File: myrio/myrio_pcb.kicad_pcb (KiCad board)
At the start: 4 copper layers, 191.1 x 89.5 mm, 136 parts, among them J1 DB9, P1 CONN_02X17, P2 CONN_02X17, Q1 PN2222A, Q10 PN2222A, Q11 PN2222A, Q12 PN2222A, Q13 PN2222A, Q14 PN2222A, Q15 PN2222A, Q16 PN2222A, Q17 PN2222A, Q18 PN2222A, Q19 PN2222A, Q2 PN2222A, Q20 PN2222A, Q21 PN2222A, Q3 PN2222A, Q4 PN2222A, Q5 PN2222A, Q6 PN2222A, Q7 PN2222A, Q8 PN2222A, Q9 PN2222A, U1 stacked-DB9, U10 INA219, U11 INA219, U13 INA219, U14 stacked-rj45-LED, U15 stacked-rj45-LED, U16 12V regulator, U2 stacked-DB9, U3 stacked-rj45-LED, U4 stacked-rj45-LED, U5 stacked-rj45-LED, U6 BNO055, U7 stacked-rj45-LED, U9 LM1084IT-5.0/NOPB

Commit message: moved the readme over here
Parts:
- removed C1, C2, C3, C4: CP1, Capacitors_THT:CP_Radial_Tantal_D4.5mm_P2.50mm
- removed D23: D, Diodes_THT:D_DO-35_SOD27_P5.08mm_Vertical_AnodeUp
- removed Q21: PN2222A, footprints:pn2222
- removed R21: 100K, Resistors_THT:R_Axial_DIN0204_L3.6mm_D1.6mm_P5.08mm_Horizontal
- removed R31: R, Resistors_THT:R_Axial_DIN0204_L3.6mm_D1.6mm_P5.08mm_Horizontal
- removed RE21: relay, footprints:relay
- removed the REF** at (198.1, 47.0)
- removed the REF** at (30.5, 48.9)
- removed the REF** at (198.8, 101.6)
- removed the REF** at (37.5, 101.6)
- removed U16: 12V regulator, TO_SOT_Packages_THT:TO-220_Vertical
- removed U9: LM1084IT-5.0/NOPB, TO_SOT_Packages_THT:TO-220_Vertical
- added J2: CONN_02X03, Pin_Headers:Pin_Header_Straight_2x03_Pitch2.54mm, F.Cu at (209.6, 74.9)
- added J3: CONN_02X03, Pin_Headers:Pin_Header_Straight_2x03_Pitch2.54mm, F.Cu at (209.6, 64.8)
- added J4: CONN_02X03, Pin_Headers:Pin_Header_Straight_2x03_Pitch2.54mm, F.Cu at (209.6, 54.6)
- added REF**: 1pin, Connectors:1pin, F.Cu at (24.1, 48.3)
- added REF**: 1pin, Connectors:1pin, F.Cu at (201.9, 45.7)
- added REF**: 1pin, Connectors:1pin, F.Cu at (38.7, 101.6)
- added REF**: 1pin, Connectors:1pin, F.Cu at (226.1, 101.0)
- added S11: 2pinscrew, footprints:screwinconnector++, F.Cu at (226.7, 59.1)
- added U8: stacked-DB9, footprints:DB9-doublestacked_PR, F.Cu at (208.5, 33.5)
- H1: footprint footprints:bmp180_ref -> footprints:bmp180
- J1: value DB9 -> CONN_02X03; footprint Connectors:DB9FD -> Pin_Headers:Pin_Header_Straight_2x03_Pitch2.54mm
- Q1, Q10, Q11, Q12, Q13, Q14, Q15, Q16, Q17, Q18, Q19, Q2, Q20, Q3, Q4, Q5, Q6, Q7, Q8, Q9: footprint footprints:pn2222 -> TO_SOT_Packages_THT:TO-92_Inline_Narrow_Oval
- S1, S10, S2, S3, S4, S5, S6, S7, S8, S9: footprint footprints:screwinconnector -> footprints:screwinconnector++
- U14, U15, U3, U4, U5, U7: footprint footprints:stacked-rj45_Final -> footprints:stacked-rj45_Final++
- moved S10 204.9 mm to (226.7, 93.3)
- moved S9 204.8 mm to (226.7, 81.9)
- moved S8 204.7 mm to (226.7, 70.5)
- moved S2 184.4 mm to (23.7, 85.6)
- moved S5 183.8 mm to (23.7, 74.2), turned to 270 degrees
- moved S4 183.5 mm to (23.7, 62.7)
- moved J1 58.6 mm to (209.6, 85.1), turned to 0 degrees
- moved S1 48.9 mm to (214.0, 102.2), turned to 0 degrees
- moved D21 20.0 mm to (169.2, 99.8), turned to 180 degrees
- moved S7 14.0 mm to (191.1, 102.2)
- moved S3 12.7 mm to (179.7, 102.2)
- moved D22 11.3 mm to (201.9, 87.6), turned to 270 degrees
- moved U1 7.63 mm to (154.3, 39.0)
- moved U2 7.63 mm to (188.0, 39.0)
- moved U15 6.99 mm to (132.1, 30.5)
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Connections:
- 220ohm1 pad 2: friction_gnd -> DGND
- 220ohm2 pad 2: friction_gnd -> DGND
- 220ohm3 pad 2: friction_gnd -> DGND
- 220ohm4 pad 2: friction_gnd -> DGND
- J1 pad 1: Net-(J1-Pad1) -> non_critical_scl
- J1 pad 2: Net-(J1-Pad2) -> i2c_scl_2
- J1 pad 3: Net-(J1-Pad3) -> tof_scl
- J1 pad 4: Net-(J1-Pad4) -> tof_scl
- J1 pad 5: friction_gnd -> (no net)
- J1 pad 6: Net-(J1-Pad6) -> critical_scl
- P1 pad 1: Net-(P1-Pad1) -> (no net)
- P1 pad 10: Net-(P1-Pad10) -> (no net)
- P1 pad 12: friction_gnd -> DGND
- P1 pad 14: Net-(P1-Pad14) -> (no net)
- P1 pad 16: friction_gnd -> DGND
- P1 pad 2: Net-(P1-Pad2) -> (no net)
- P1 pad 20: friction_gnd -> DGND
- P1 pad 24: friction_gnd -> DGND
- P1 pad 28: friction_gnd -> DGND
- P1 pad 30: friction_gnd -> DGND
- P1 pad 33: Net-(P1-Pad33) -> (no net)
- P1 pad 4: Net-(P1-Pad4) -> (no net)
- P1 pad 6: friction_gnd -> DGND
- P1 pad 8: friction_gnd -> DGND
- P2 pad 1: Net-(P2-Pad1) -> (no net)
- P2 pad 10: Net-(P2-Pad10) -> (no net)
- P2 pad 14: Net-(P2-Pad14) -> (no net)
- P2 pad 2: Net-(P2-Pad2) -> (no net)
- P2 pad 33: Net-(P2-Pad33) -> (no net)
- P2 pad 4: Net-(P2-Pad4) -> (no net)
- P2 pad 6: friction_gnd -> DGND
- P2 pad 7: Net-(P2-Pad7) -> (no net)
- P2 pad 9: Net-(P2-Pad9) -> (no net)
- Q1 pad 1: friction_gnd -> DGND
- Q10 pad 1: friction_gnd -> DGND
- Q11 pad 1: friction_gnd -> DGND
- Q12 pad 1: friction_gnd -> DGND
- Q13 pad 1: friction_gnd -> DGND
- Q14 pad 1: friction_gnd -> DGND
- Q15 pad 1: friction_gnd -> DGND
- Q16 pad 1: friction_gnd -> DGND
- Q17 pad 1: friction_gnd -> DGND
- Q18 pad 1: friction_gnd -> DGND
- Q19 pad 1: friction_gnd -> DGND
- Q2 pad 1: friction_gnd -> DGND
- Q20 pad 1: friction_gnd -> DGND
- Q3 pad 1: friction_gnd -> DGND
- Q4 pad 1: friction_gnd -> DGND
- Q5 pad 1: friction_gnd -> DGND
- Q6 pad 1: friction_gnd -> DGND
- Q7 pad 1: friction_gnd -> DGND
- Q8 pad 1: friction_gnd -> DGND
- Q9 pad 1: friction_gnd -> DGND
- RE1 pad 5: Net-(RE1-Pad5) -> (no net)
- RE10 pad 5: Net-(RE10-Pad5) -> (no net)
- RE11 pad 5: Net-(RE11-Pad5) -> (no net)
- RE12 pad 5: Net-(RE12-Pad5) -> (no net)
- RE13 pad 6: Net-(RE13-Pad6) -> (no net)
- RE15 pad 6: Net-(RE15-Pad6) -> (no net)
- RE18 pad 10: Net-(RE18-Pad10) -> (no net)
- RE19 pad 1: friction_gnd -> DGND
- RE2 pad 5: Net-(RE2-Pad5) -> (no net)
- RE20 pad 1: friction_gnd -> DGND
- RE3 pad 5: Net-(RE3-Pad5) -> (no net)
- RE4 pad 5: Net-(RE4-Pad5) -> (no net)
- RE5 pad 1: Net-(RE5-Pad1) -> (no net)
- RE9 pad 5: Net-(RE9-Pad5) -> (no net)
- S1 pad 1: VCC_IN -> batt_in
- S1 pad 2: friction_gnd -> DGND
- S10 pad 1: 5V -> 12V
- S10 pad 2: friction_gnd -> DGND
- S6 pad 2: friction_gnd -> DGND
- S7 pad 1: motor_pwr -> 24V
- S7 pad 2: friction_gnd -> magnetic_pwr
- S8 pad 1: VCC_IN -> 12V
- S8 pad 2: friction_gnd -> DGND
- S9 pad 1: 12V -> DGND
- S9 pad 2: friction_gnd -> 24V
- U1 pad 14: friction_gnd -> DGND
- U1 pad 15: friction_gnd -> DGND
- U1 pad 16: friction_gnd -> DGND
- U1 pad 17: friction_gnd -> DGND
- U1 pad 18: friction_gnd -> DGND
- U1 pad 5: friction_gnd -> DGND
- U1 pad 6: friction_gnd -> DGND
- U1 pad 7: friction_gnd -> DGND
- U1 pad 8: friction_gnd -> DGND
- U1 pad 9: friction_gnd -> DGND
- U10 pad 5: Net-(U10-Pad5) -> (no net)
- U10 pad 6: Net-(U10-Pad6) -> (no net)
- U11 pad 5: Net-(U11-Pad5) -> (no net)
- U11 pad 6: Net-(U11-Pad6) -> (no net)
- U11 pad 7: 24V -> 12V
- U11 pad 8: VCC_IN -> batt_in
- U13 pad 5: Net-(U13-Pad5) -> (no net)
- U13 pad 6: Net-(U13-Pad6) -> (no net)
- U14 pad 14: Net-(U14-Pad14) -> (no net)
- U14 pad 17: Net-(U14-Pad17) -> (no net)
- U14 pad 18: Net-(U14-Pad18) -> (no net)
- U14 pad 19: Net-(U14-Pad19) -> (no net)
- U14 pad 20: Net-(U14-Pad20) -> (no net)
- U14 pad 21: Net-(U14-Pad21) -> (no net)
- U14 pad 22: Net-(U14-Pad22) -> (no net)
- U14 pad 23: Net-(U14-Pad23) -> (no net)
- U14 pad 24: Net-(U14-Pad24) -> (no net)
- U14 pad 6: Net-(U14-Pad6) -> (no net)
- U14 pad 8: Net-(U14-Pad8) -> (no net)
- U15 pad 12: Net-(U15-Pad12) -> (no net)
- U15 pad 13: Net-(U15-Pad13) -> (no net)
- U15 pad 15: Net-(U15-Pad15) -> (no net)
- U15 pad 16: Net-(U15-Pad16) -> (no net)
- U15 pad 17: Net-(U15-Pad17) -> (no net)
- U15 pad 18: Net-(U15-Pad18) -> (no net)
- U15 pad 19: Net-(U15-Pad19) -> (no net)
- U15 pad 20: Net-(U15-Pad20) -> (no net)
- U15 pad 21: Net-(U15-Pad21) -> (no net)
- U15 pad 22: Net-(U15-Pad22) -> (no net)
- U15 pad 23: Net-(U15-Pad23) -> (no net)
- U15 pad 24: Net-(U15-Pad24) -> (no net)
- U2 pad 14: friction_gnd -> DGND
- U2 pad 15: friction_gnd -> DGND
- U2 pad 16: friction_gnd -> DGND
- U2 pad 17: friction_gnd -> DGND
- U2 pad 18: friction_gnd -> DGND
- U2 pad 5: friction_gnd -> DGND
- U2 pad 6: friction_gnd -> DGND
- U2 pad 7: friction_gnd -> DGND
- U2 pad 8: friction_gnd -> DGND
- U2 pad 9: friction_gnd -> DGND
- U3 pad 17: Net-(U3-Pad17) -> (no net)
- U3 pad 18: Net-(U3-Pad18) -> (no net)
- U3 pad 19: Net-(U3-Pad19) -> (no net)
- U3 pad 20: Net-(U3-Pad20) -> (no net)
- U3 pad 21: Net-(U3-Pad21) -> (no net)
- U3 pad 22: Net-(U3-Pad22) -> (no net)
- U3 pad 23: Net-(U3-Pad23) -> (no net)
- U3 pad 24: Net-(U3-Pad24) -> (no net)
- U4 pad 11: non_critical_scl -> tof_scl
- U4 pad 14: non_critical_sda -> tof_sda
- U4 pad 15: non_critical_scl -> tof_scl
- U4 pad 16: non_critical_sda -> tof_sda
- U4 pad 17: Net-(U4-Pad17) -> (no net)
- U4 pad 18: Net-(U4-Pad18) -> (no net)
- U4 pad 19: Net-(U4-Pad19) -> (no net)
- U4 pad 20: Net-(U4-Pad20) -> (no net)
- U4 pad 21: Net-(U4-Pad21) -> (no net)
- U4 pad 22: Net-(U4-Pad22) -> (no net)
- U4 pad 23: Net-(U4-Pad23) -> (no net)
- U4 pad 24: Net-(U4-Pad24) -> (no net)
- U4 pad 3: critical_scl -> tof_scl
- U4 pad 6: critical_sda -> tof_sda
- U4 pad 7: non_critical_scl -> tof_scl
- U4 pad 8: non_critical_sda -> tof_sda
- U5 pad 11: non_critical_scl -> stress_scl
- U5 pad 14: non_critical_sda -> stress_sda
- U5 pad 15: non_critical_scl -> stress_scl
- U5 pad 16: non_critical_sda -> stress_sda
- U5 pad 17: Net-(U5-Pad17) -> (no net)
- U5 pad 18: Net-(U5-Pad18) -> (no net)
- U5 pad 19: Net-(U5-Pad19) -> (no net)
- U5 pad 20: Net-(U5-Pad20) -> (no net)
- U5 pad 21: Net-(U5-Pad21) -> (no net)
- U5 pad 22: Net-(U5-Pad22) -> (no net)
- U5 pad 23: Net-(U5-Pad23) -> (no net)
- U5 pad 24: Net-(U5-Pad24) -> (no net)
- U5 pad 3: critical_scl -> stress_scl
- U5 pad 6: critical_sda -> stress_sda
- U5 pad 7: non_critical_scl -> stress_scl
- U5 pad 8: non_critical_sda -> stress_sda
- U6 pad 10: Net-(U6-Pad10) -> (no net)
- U6 pad 2: Net-(U6-Pad2) -> (no net)
- U6 pad 6: Net-(U6-Pad6) -> (no net)
- U6 pad 7: Net-(U6-Pad7) -> (no net)
- U6 pad 8: Net-(U6-Pad8) -> (no net)
- U6 pad 9: Net-(U6-Pad9) -> (no net)
- U7 pad 14: Net-(U7-Pad14) -> (no net)
- U7 pad 16: Net-(U7-Pad16) -> (no net)
- U7 pad 17: Net-(U7-Pad17) -> (no net)
- U7 pad 18: Net-(U7-Pad18) -> (no net)
- U7 pad 19: Net-(U7-Pad19) -> (no net)
- U7 pad 20: Net-(U7-Pad20) -> (no net)
- U7 pad 21: Net-(U7-Pad21) -> (no net)
- U7 pad 22: Net-(U7-Pad22) -> (no net)
- U7 pad 23: Net-(U7-Pad23) -> (no net)
- U7 pad 24: Net-(U7-Pad24) -> (no net)
- U7 pad 4: Net-(U7-Pad4) -> (no net)
- U7 pad 5: Net-(U7-Pad5) -> (no net)
- U7 pad 6: Net-(U7-Pad6) -> (no net)
- U7 pad 7: Net-(U7-Pad7) -> (no net)
- U7 pad 8: Net-(U7-Pad8) -> (no net)
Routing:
- net VCC_IN: track 252.3 -> 0.00 mm, vias 8 -> 0
- net tof_scl: track 0.00 -> 232.0 mm, vias 0 -> 3
- net tof_sda: track 0.00 -> 216.9 mm, vias 0 -> 6
- net stress_scl: track 0.00 -> 212.6 mm, vias 0 -> 3
- net stress_sda: track 0.00 -> 209.0 mm, vias 0 -> 2
- net friction_gnd: track 195.1 -> 0.00 mm, vias 5 -> 0
- net A0: track 203.5 -> 45.1 mm, vias 1 -> 2
- net critical_sda: track 151.8 -> 307.0 mm, vias 4 -> 6
- net A1: track 197.0 -> 43.5 mm, vias 1 -> 3
- net critical_scl: track 152.4 -> 296.7 mm, vias 1 -> 4
- net i2c_sda_2: track 167.9 -> 279.5 mm, vias 5 -> 7
- net i2c_scl_2: track 179.6 -> 289.1 mm, vias 5 -> 8
- net motor_ctrl: track 55.7 -> 152.5 mm, vias 5 -> 3
- net motor_pwr: track 96.0 -> 0.00 mm, vias 2 -> 0
- net 24V: track 86.6 -> 6.35 mm, vias 3 -> 1
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- added copper zone on B.Cu, net 24V
- removed copper zone on F.Cu, net 24V
- removed copper zone on B.Cu, net friction_gnd
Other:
- board size 191.1 x 89.5 mm -> 212 x 89.5 mm
- board text added: "Battery Sensor"
- board text added: "Brake Sensor"
- board text added: "Josh Cristol Cody Horton"
- board text added: "Mpwr"
- board text added: "MyRio Sensor"
- board text added: "NonC"
- board text added: "SCL2"
- board text added: "SCL3"
- board text added: "SDA2"
- board text added: "SDA3"
- board text added: "WE BUILD SHIT"
- board text added: "Zener Diode"
- board text added: "crit"
- board text added: "myRio+"
- board text added: "scl"
- board text added: "sda"
- board text added: "stress"
- board text added: "tof"
- board text added: "vcc"
- board text removed: "Dgnd"
- board text removed: "Motor"
- board text removed: "Regulator"
- board text removed: "WE BUILD SHIT."
- board text removed: "a0 a1 4 digital i2c lines"
- board text removed: "cap gnd move next to motor gnd screw terminals"
- board text removed: "myRio"
- board text removed: "power- battery connection and converters battery+ bat- 4 connectors for 24V booster 4 connectors for 5V booster"
- board text removed: "scl3"
- board text removed: "sda3"

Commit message: layout done, still tracing
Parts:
- removed D21: ZENER, Discret:D3
- removed the REF** at (24.1, 48.3)
- removed the REF** at (201.9, 45.7)
- removed the REF** at (38.7, 101.6)
- removed the REF** at (226.1, 101.0)
- removed S10, S11, S3, S7, S8, S9: 2pinscrew, footprints:screwinconnector++
- added D23: LED, LEDs:LED_D5.0mm, F.Cu at (212.1, 90.7)
- added R21: 500, Resistors_THT:R_Axial_DIN0204_L3.6mm_D1.6mm_P5.08mm_Horizontal, F.Cu at (208.1, 88.2)
- added R31: 12K, Resistors_THT:R_Axial_DIN0204_L3.6mm_D1.6mm_P5.08mm_Horizontal, F.Cu at (32.0, 95.2)
- added R32: 2K, Resistors_THT:R_Axial_DIN0204_L3.6mm_D1.6mm_P5.08mm_Horizontal, F.Cu at (37.0, 98.2)
- added R33: 2K, Resistors_THT:R_Axial_DIN0204_L3.6mm_D1.6mm_P5.08mm_Horizontal, F.Cu at (37.1, 104.8)
- added REF**: 1pin, Connectors:1pin, F.Cu at (23.1, 106.2)
- added REF**: 1pin, Connectors:1pin, F.Cu at (235.1, 106.2)
- added REF**: 1pin, Connectors:1pin, F.Cu at (23.1, 48.2)
- added REF**: 1pin, Connectors:1pin, F.Cu at (223.1, 46.2)
- added T1: Phoenix_Contact_1935187, footprints:Phoenix_Contact_1935187, F.Cu at (230.1, 83.7)
- added T2: Phoenix_Contact_1935187, footprints:Phoenix_Contact_1935187, F.Cu at (191.8, 100.2)
- added T3: Phoenix_Contact_1935187, footprints:Phoenix_Contact_1935187, F.Cu at (230.1, 63.2)
- added T4: Phoenix_Contact_1935187, footprints:Phoenix_Contact_1935187, F.Cu at (212.1, 100.2)
- P1, P2: moved to B.Cu
- R30: value R -> 12K
- S1: value 2pinscrew -> L101011MS02Q; footprint footprints:screwinconnector++ -> footprints:L101011MS02Q
- moved P1 65.9 mm to (169.4, 102.0)
- moved P2 65.9 mm to (112.2, 102.0)
- moved R29 59.7 mm to (42.0, 100.2), turned to 270 degrees
- moved R28 59.2 mm to (45.0, 100.2), turned to 270 degrees
- moved R22 26.1 mm to (63.0, 100.2), turned to 270 degrees
- moved S1 24.9 mm to (238.1, 95.7), turned to 90 degrees
- moved R23 21.5 mm to (60.0, 100.2), turned to 270 degrees
- moved R30 19.6 mm to (32.0, 102.2)
- moved S6 19.2 mm to (183.6, 105.2)
- moved U8 14.2 mm to (221.6, 39.0), turned to 180 degrees
- moved R24 11.0 mm to (51.0, 100.2), turned to 270 degrees
- moved R26 9.71 mm to (57.0, 100.2), turned to 270 degrees
- moved J1 7.02 mm to (210.1, 78.1)
- moved J2 7.02 mm to (210.1, 67.9)
- moved J4 7.02 mm to (210.1, 47.6)
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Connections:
- net batt_in renamed battery_sensor_input
- net laser_digital renamed laser_digital1
- net main_laser renamed main_laser1
- P2 pad 7: (no net) -> laser_digital2
- RE1 pad 1: 5V -> DGND
- RE1 pad 10: DGND -> 5V
- RE10 pad 1: 5V -> DGND
- RE10 pad 10: DGND -> 5V
- RE11 pad 1: 5V -> DGND
- RE11 pad 10: DGND -> 5V
- RE12 pad 1: 5V -> DGND
- RE12 pad 10: DGND -> 5V
- RE17 pad 1: 5V -> DGND
- RE17 pad 10: DGND -> 5V
- RE18 pad 1: to_cap -> (no net)
- RE18 pad 10: (no net) -> to_cap
- RE2 pad 1: 5V -> DGND
- RE2 pad 10: DGND -> 5V
- RE3 pad 1: 5V -> DGND
- RE3 pad 10: DGND -> 5V
- RE4 pad 1: 5V -> DGND
- RE4 pad 10: DGND -> 5V
- RE6 pad 1: 2way_open_1 -> 2way_close_1
- RE6 pad 10: 2way_close_1 -> 2way_open_1
- RE7 pad 1: 2way_open_2 -> 2way_close_2
- RE7 pad 10: 2way_close_2 -> 2way_open_2
- RE8 pad 1: 2way_open_3 -> 2way_close_3
- RE8 pad 10: 2way_close_3 -> 2way_open_3
- RE9 pad 1: 5V -> DGND
- RE9 pad 10: DGND -> 5V
- S1 pad 2: DGND -> battery+fuse
- U7 pad 4: (no net) -> 24V
- U7 pad 5: (no net) -> DGND
- U7 pad 7: (no net) -> main_laser2
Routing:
- net critical_sda: track 307.0 -> 19.3 mm, vias 6 -> 0
- net i2c_scl_2: track 289.1 -> 34.9 mm, vias 8 -> 0
- net i2c_sda_2: track 279.5 -> 26.4 mm, vias 7 -> 0
- net critical_scl: track 296.7 -> 96.2 mm, vias 4 -> 2
- net tof_sda: track 216.9 -> 21.2 mm, vias 6 -> 1
- net stress_scl: track 212.6 -> 22.5 mm, vias 3 -> 0
- net tof_scl: track 232.0 -> 78.2 mm, vias 3 -> 1
- net motor_ctrl: track 152.5 -> 0.00 mm, vias 3 -> 0
- net non_critical_sda: track 307.3 -> 178.0 mm, vias 8 -> 5
- net laser_digital1: track 123.4 -> 2.61 mm, vias 3 -> 0
- net laser2: track 96.6 -> 0.00 mm, vias 4 -> 0
- net sense_pwr_ctrl: track 89.4 -> 0.00 mm, vias 5 -> 0
- net pressure_activation: track 85.5 -> 0.06 mm, vias 3 -> 0
- net magnetic_ctrl: track 83.6 -> 0.00 mm, vias 1 -> 0
- net to_cap_ctrl: track 78.5 -> 0.00 mm, vias 1 -> 0
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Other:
- board size 212 x 89.5 mm -> 220 x 93.5 mm
- net class Power: trace_width 0.381 -> 0.508
- board text added: "12K"
- board text added: "2K"
- board text added: "500"
- board text added: "Fuse \/ \/"
- board text added: "I2C Pullups"
- board text added: "RIO+"
- board text added: "RIO-"
- board text removed: "Mpwr"
- board text removed: "Zener Diode"
- board text removed: "myRio+"

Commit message: considering capacitors
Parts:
- removed REF** (x4): 1pin, Connectors:1pin
- added C1: C, Capacitors_THT:CP_Radial_D5.0mm_P2.50mm, F.Cu at (221.1, 81.2)
- added C2: C, Capacitors_THT:CP_Radial_D5.0mm_P2.50mm, F.Cu at (195.4, 133.5)
- added C3: C, Capacitors_THT:CP_Radial_D5.0mm_P2.50mm, F.Cu at (222.5, 140.2)
- added C4: C, Capacitors_THT:CP_Radial_D5.0mm_P2.50mm, F.Cu at (210.8, 133.3)
- added C5: C, Capacitors_THT:CP_Radial_D5.0mm_P2.50mm, F.Cu at (167.6, 127.9)
- added C6: C, Capacitors_THT:CP_Radial_D5.0mm_P2.50mm, F.Cu at (147.2, 123.4)
- added C7, C8, C9: C, Capacitors_THT:CP_Radial_D5.0mm_P2.50mm, F.Cu at (129.1, 120.3)
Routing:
- net critical_sda: track 19.3 -> 325.5 mm, vias 0 -> 4
- net i2c_sda_2: track 26.4 -> 291.2 mm, vias 0 -> 3
- net i2c_scl_2: track 34.9 -> 285.1 mm, vias 0 -> 4
- net tof_sda: track 21.2 -> 248.4 mm, vias 1 -> 4
- net critical_scl: track 96.2 -> 321.8 mm, vias 2 -> 4
- net stress_scl: track 22.5 -> 201.8 mm, vias 0 -> 3
- net motor_ctrl: track 0.00 -> 157.1 mm, vias 0 -> 1
- net tof_scl: track 78.2 -> 230.4 mm, vias 1 -> 2
- net main_laser2: track 0.00 -> 121.9 mm, vias 0 -> 1
- net non_critical_sda: track 178.0 -> 291.9 mm, vias 5 -> 8
- net A0: track 0.00 -> 97.9 mm, vias 0 -> 2
- net A1: track 0.36 -> 93.4 mm, vias 0 -> 1
- net magnetic_ctrl: track 0.00 -> 88.3 mm, vias 0 -> 1
- net sense_pwr_ctrl: track 0.00 -> 87.7 mm, vias 0 -> 2
- net laser2: track 0.00 -> 79.6 mm, vias 0 -> 2
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
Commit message: traces for days
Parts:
- removed C8: C, Capacitors_THT:CP_Radial_D5.0mm_P2.50mm
- moved C7 70.2 mm to (184.3, 76.9)
- moved C4 67.9 mm to (221.1, 66.2)
- moved C2 63.8 mm to (165.1, 77.4)
- moved C3 59.3 mm to (177.1, 102.2), turned to 270 degrees
- moved C6 58.3 mm to (123.5, 70.2)
- moved C5 44.6 mm to (165.1, 83.4), turned to 270 degrees
- moved C9 42.7 mm to (141.4, 79.4), turned to 90 degrees
- moved P1 40.7 mm to (128.8, 104.5), turned to 270 degrees
- moved P2 40.7 mm to (71.6, 104.5), turned to 270 degrees
- moved R27 9.50 mm to (63.5, 100.2)
- moved R29 9.50 mm to (51.5, 100.2)
- moved R22 8.50 mm to (54.5, 100.2)
- moved R24 8.50 mm to (42.5, 100.2)
- moved R26 3.50 mm to (60.5, 100.2)
- moved R28 3.50 mm to (48.5, 100.2)
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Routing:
- net critical_sda: track 325.5 -> 102.8 mm, vias 4 -> 2
- net critical_scl: track 321.8 -> 100.3 mm, vias 4 -> 0
- net i2c_scl_2: track 285.1 -> 63.6 mm, vias 4 -> 0
- net i2c_sda_2: track 291.2 -> 87.9 mm, vias 3 -> 0
- net motor_ctrl: track 157.1 -> 69.5 mm
- net sense_pwr_ctrl: track 87.7 -> 1.79 mm, vias 2 -> 0
- net to_cap_ctrl: track 66.7 -> 0.00 mm, vias 1 -> 0
- net laser_digital1: track 58.6 -> 2.61 mm
- net i2c_scl_3: track 155.4 -> 107.5 mm, vias 2 -> 0
- net pressure_activation: track 71.9 -> 107.7 mm
- net laser_digital2: track 81.9 -> 49.4 mm
- net magnetic_ctrl: track 88.3 -> 55.8 mm
- net friction_ctrl: track 78.3 -> 45.8 mm
- net pressure1-: track 134.2 -> 103.5 mm
- net pressure2-: track 106.0 -> 76.4 mm
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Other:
- net class Default: via_dia 0.889 -> 0.762
- net class HighCurrent: via_dia 0.889 -> 0.762
- net class Power: via_dia 0.889 -> 0.762
- rule via_min_size: 0.781 -> 0.762

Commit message: more traces done
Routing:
- net critical_sda: track 102.8 -> 330.9 mm, vias 2 -> 5
- net critical_scl: track 100.3 -> 316.4 mm, vias 0 -> 3
- net i2c_scl_2: track 63.6 -> 279.3 mm, vias 0 -> 5
- net i2c_sda_2: track 87.9 -> 295.5 mm, vias 0 -> 4
- net motor_ctrl: track 69.5 -> 144.5 mm, vias 1 -> 3
- net sense_pwr_ctrl: track 1.79 -> 65.8 mm, vias 0 -> 2
- net i2c_scl_3: track 107.5 -> 165.3 mm, vias 0 -> 2
- net laser_digital1: track 2.61 -> 58.9 mm, vias 0 -> 1
- net to_cap_ctrl: track 0.00 -> 51.7 mm, vias 0 -> 1
- net pressure4-: track 98.4 -> 148.8 mm, vias 2 -> 4
- net pressure3-: track 68.1 -> 118.0 mm, vias 3 -> 5
- net pressure2-: track 76.4 -> 124.8 mm, vias 1 -> 3
- net laser1: track 43.8 -> 92.2 mm
- net i2c_sda_3: track 212.1 -> 164.6 mm, vias 2 -> 1
- net laser2: track 51.4 -> 89.8 mm
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
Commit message: made small changes according to feedback
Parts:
- moved C3 58.6 mm to (235.4, 97.8)
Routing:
- net battery: track 40.5 -> 37.4 mm
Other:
- board text added: "Critical"
- board text added: "I2C_2"
- board text added: "I2C_3"
- board text added: "Lasers"
- board text added: "Non-Critical"
- board text added: "NonCrit"
- board text added: "Pneu 1"
- board text added: "Pneu 2"
- board text added: "ToF1"
- board text added: "ToF2"

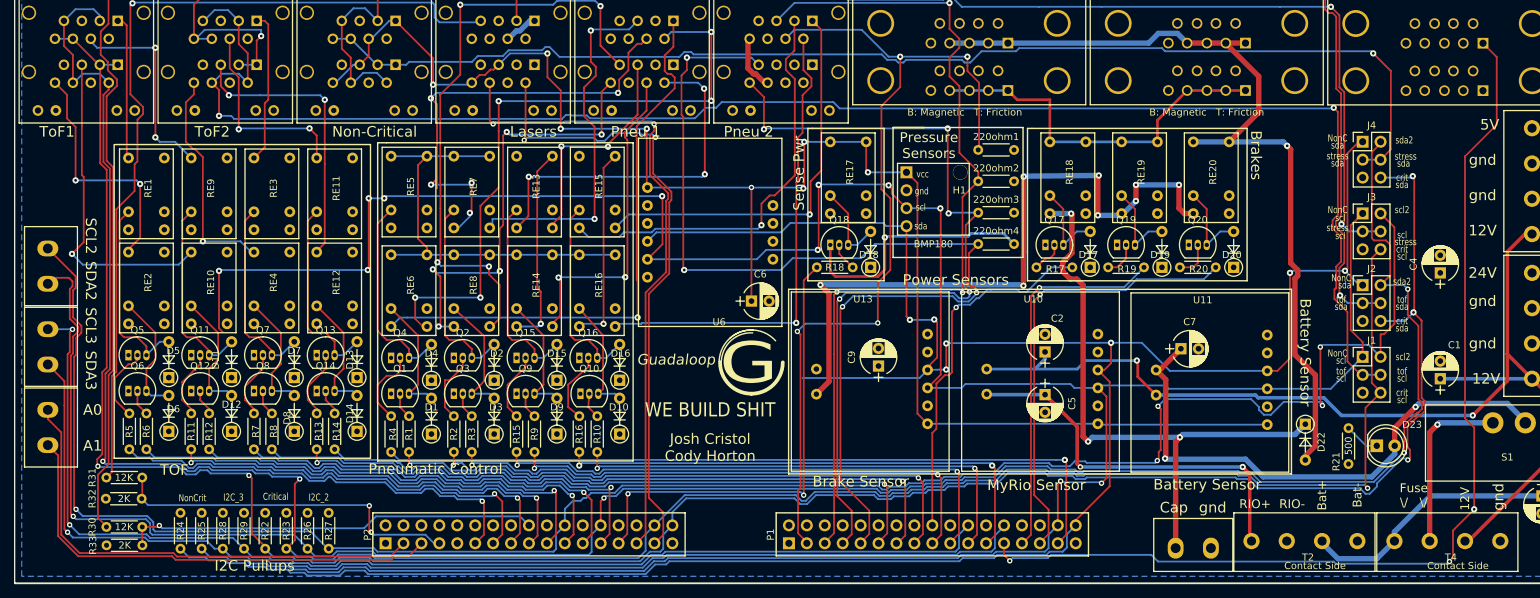
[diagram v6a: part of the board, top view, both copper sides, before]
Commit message: made changes according to 7-31 feedback doc
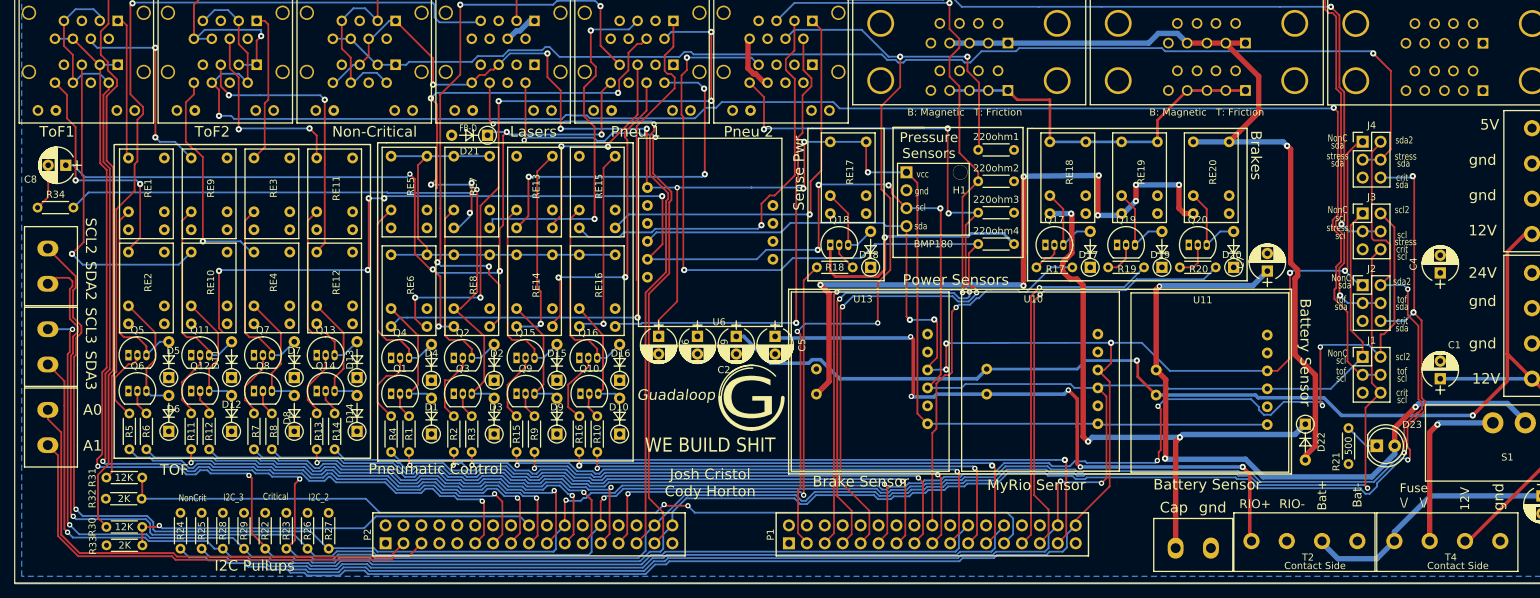
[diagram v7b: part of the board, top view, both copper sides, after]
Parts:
- added C8: C, Capacitors_THT:CP_Radial_D5.0mm_P2.50mm, F.Cu at (26.3, 50.9)
- added D21: D, Diodes_THT:D_DO-35_SOD27_P5.08mm_Vertical_AnodeUp, F.Cu at (86.0, 46.7)
- added R34: R, Resistors_THT:R_Axial_DIN0204_L3.6mm_D1.6mm_P5.08mm_Horizontal, F.Cu at (22.3, 56.9)
- moved C2 43.8 mm to (121.3, 75.2), turned to 270 degrees
- moved C5 39.1 mm to (126.8, 75.2)
- moved C9 26.0 mm to (115.8, 75.2), turned to 270 degrees
- moved C7 16.5 mm to (196.6, 65.9), turned to 90 degrees
- moved C6 14.1 mm to (110.3, 75.2), turned to 270 degrees
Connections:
- P1 pad 25: motor_ctrl -> laser_digital2
- P2 pad 7: laser_digital2 -> (no net)
- U8 pad 10: motor_ctrl -> (no net)
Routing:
- net motor_ctrl: track 144.5 -> 0.00 mm, vias 3 -> 0
- net laser_digital2: track 49.9 -> 132.7 mm
- net 2way_ctrl_3_coil-: track 18.1 -> 95.4 mm, vias 0 -> 1
- net 2way_open_3: track 62.5 -> 130.1 mm, vias 5 -> 6
- net myRIO_12V: track 54.6 -> 96.5 mm, vias 2 -> 5
- net 12V: track 153.5 -> 189.4 mm
- net battery_sensor_input: track 77.8 -> 101.8 mm, vias 2 -> 3
- net non_critical_sda: track 344.3 -> 326.1 mm
- net Net-(C8-Pad2): track 0.00 -> 6.62 mm
- net sense_pwr: track 223.9 -> 230.0 mm
- net i2c_scl_2: track 279.3 -> 280.0 mm, vias 5 -> 6
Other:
- board text added: "FB-D"

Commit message: donezo mcfunzo
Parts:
- removed S1: L101011MS02Q, footprints:L101011MS02Q
- added REF**: 1pin, Connectors:1pin, F.Cu at (223.7, 45.6)
- added REF**: 1pin, Connectors:1pin, F.Cu at (23.7, 48.1)
- added REF**: 1pin, Connectors:1pin, F.Cu at (23.7, 105.6)
- added REF**: 1pin, Connectors:1pin, F.Cu at (234.7, 105.6)
- added T5: Phoenix_Contact_1935187, footprints:Phoenix_Contact_1935187, F.Cu at (230.1, 102.7)
- moved C3 17.4 mm to (220.0, 89.9)
- moved C8 3.11 mm to (24.7, 53.6)
- moved T4 2.22 mm to (209.8, 100.1)
- moved S6 2.07 mm to (181.5, 105.1)
- moved T2 2.07 mm to (189.7, 100.1)
- moved R34 1.32 mm to (21.7, 58.1)
- moved T1 1.01 mm to (230.1, 82.7)
- moved T3 0.57 mm to (230.1, 62.6)
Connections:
- C7 pad 1: battery_sensor_input -> battery+fuse
- D23 pad 2: battery_sensor_input -> battery+fuse
- R34 pad 2: 2way_ctrl_3_coil- -> SolenoidPower
- RE18 pad 1: (no net) -> to_cap
- RE18 pad 10: to_cap -> (no net)
- RE8 pad 5: 24V_activation -> SolenoidPower
- RE8 pad 6: 24V_activation -> SolenoidPower
- U11 pad 8: battery_sensor_input -> battery+fuse
- U14 pad 11: DGND -> SolenoidGround
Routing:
- net SolenoidPower: track 0.00 -> 242.5 mm, vias 0 -> 4
- net SolenoidGround: track 0.00 -> 177.3 mm, vias 0 -> 1
- net battery_sensor_input: track 101.8 -> 0.00 mm, vias 3 -> 0
- net 2way_ctrl_3_coil-: track 95.4 -> 18.1 mm, vias 1 -> 0
- net battery+fuse: track 24.9 -> 92.6 mm, vias 1 -> 2
- net 24V: track 13.0 -> 56.0 mm, vias 0 -> 1
- net 12V: track 189.4 -> 179.8 mm, vias 2 -> 1
- net 24V_activation: track 60.7 -> 66.8 mm
- net Net-(C8-Pad2): track 6.62 -> 4.71 mm
- net 2way_open_3: track 130.1 -> 131.8 mm
- net battery: track 37.4 -> 36.7 mm
- net myRIO_12V: track 96.5 -> 97.1 mm
- net to_cap: track 85.9 -> 85.5 mm, vias 3 -> 2
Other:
- board text added: "SLN+"
- board text added: "SLN-"
